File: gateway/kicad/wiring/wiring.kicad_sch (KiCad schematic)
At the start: 1 part

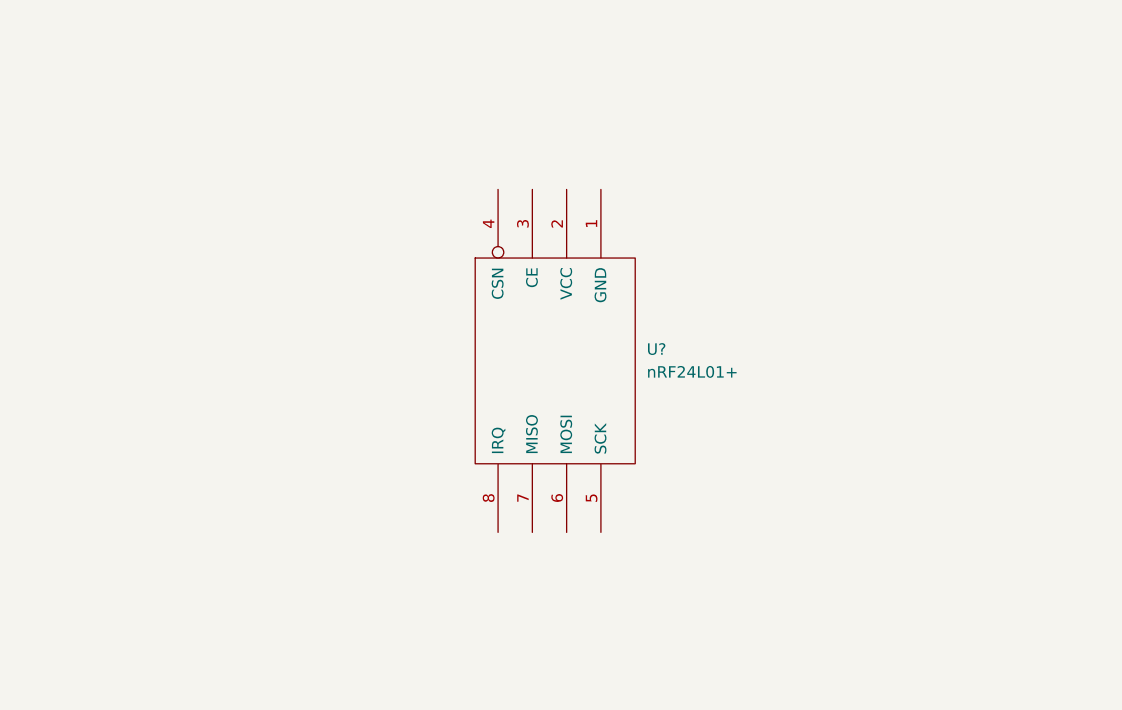
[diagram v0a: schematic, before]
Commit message: feat: wiring for gateway
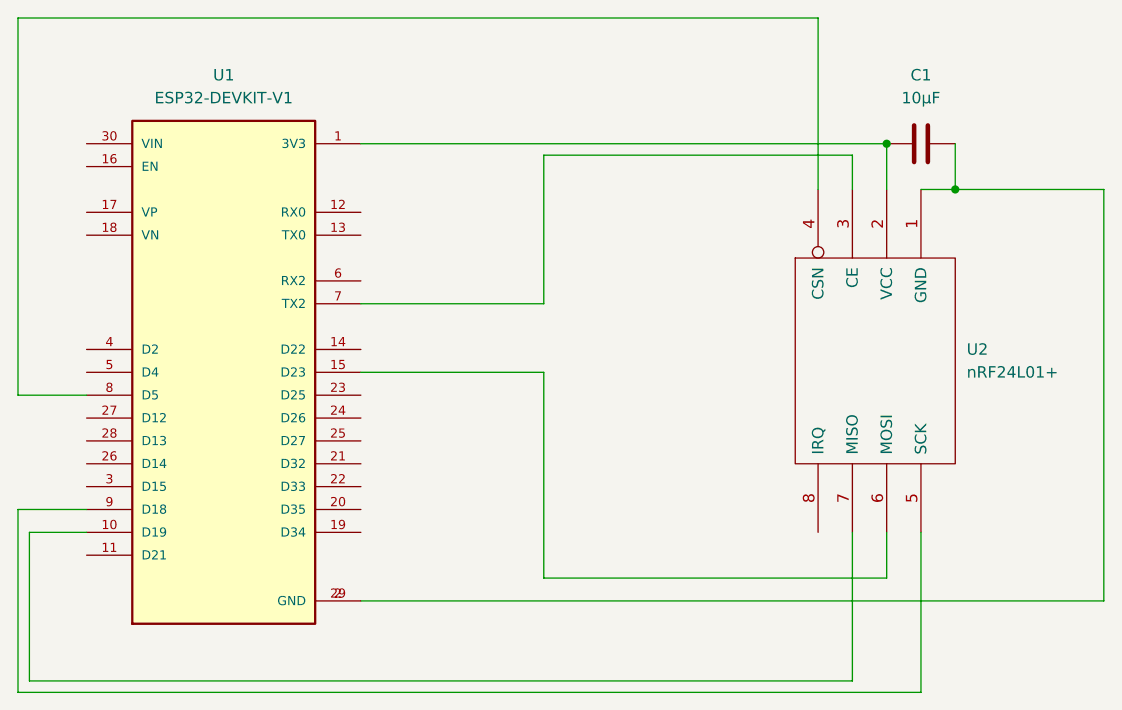
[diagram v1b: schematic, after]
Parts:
- added C1: 10µF, Capacitor_THT:C_Disc_D3.0mm_W1.6mm_P2.50mm, symbol Device:C
- added U1: ESP32-DEVKIT-V1, ESP32-DEVKIT-V1:MODULE_ESP32_DEVKIT_V1, symbol ESP32-DEVKIT-V1:ESP32-DEVKIT-V1
- gave numbers to parts that had none: 1
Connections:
- net at U2.1 (GND): now also C1.2, U1.2 (GND), U1.29 (GND)
- net at U2.2 (VCC): now also C1.1, U1.1 (3V3)
- net at U2.3 (CE): now also U1.7 (TX2)
- net at U2.4 (CSN): now also U1.8 (D5)
- net at U2.5 (SCK): now also U1.9 (D18)
- net at U2.6 (MOSI): now also U1.15 (D23)
- net at U2.7 (MISO): now also U1.10 (D19)
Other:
- moved on the sheet: U2
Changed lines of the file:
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@@
 (kicad_sch (version 20211123) (generator eeschema)
   (paper "A4")
-  (symbol (lib_id "nRF24L01+:nRF24L01+") (at 139.7 91.44 270) (unit 1)
+  (junction (at 176.53 67.31) (diameter 0) (color 0 0 0 0)
+  )
+  (junction (at 184.15 72.39) (diameter 0) (color 0 0 0 0)
+  )
+  (wire (pts (xy 138.43 85.09) (xy 138.43 68.58))
+    (stroke (width 0) (type default) (color 0 0 0 0))
+  )
+  (wire (pts (xy 118.11 67.31) (xy 176.53 67.31))
+    (stroke (width 0) (type default) (color 0 0 0 0))
+  )
+  (wire (pts (xy 138.43 92.71) (xy 138.43 115.57))
+    (stroke (width 0) (type default) (color 0 0 0 0))
+  )
+  (wire (pts (xy 172.72 68.58) (xy 172.72 72.39))
+    (stroke (width 0) (type default) (color 0 0 0 0))
+  )
+  (wire (pts (xy 184.15 67.31) (xy 184.15 72.39))
+    (stroke (width 0) (type default) (color 0 0 0 0))
+  )
+  (wire (pts (xy 138.43 68.58) (xy 172.72 68.58))
+    (stroke (width 0) (type default) (color 0 0 0 0))
+  )
+  (wire (pts (xy 200.66 118.11) (xy 200.66 72.39))
+    (stroke (width 0) (type default) (color 0 0 0 0))
+  )
+  (wire (pts (xy 184.15 72.39) (xy 180.34 72.39))
+    (stroke (width 0) (type default) (color 0 0 0 0))
+  )
+  (wire (pts (xy 200.66 72.39) (xy 184.15 72.39))
+    (stroke (width 0) (type default) (color 0 0 0 0))
+  )
+  (wire (pts (xy 118.11 92.71) (xy 138.43 92.71))
+    (stroke (width 0) (type default) (color 0 0 0 0))
+  )
+  (wire (pts (xy 81.28 127) (xy 172.72 127))
+    (stroke (width 0) (type default) (color 0 0 0 0))
+  )
+  (wire (pts (xy 80.01 128.27) (xy 180.34 128.27))
+    (stroke (width 0) (type default) (color 0 0 0 0))
+  )
+  (wire (pts (xy 138.43 115.57) (xy 176.53 115.57))
+    (stroke (width 0) (type default) (color 0 0 0 0))
+  )
+  (wire (pts (xy 176.53 67.31) (xy 176.53 72.39))
+    (stroke (width 0) (type default) (color 0 0 0 0))
+  )
+  (wire (pts (xy 118.11 118.11) (xy 200.66 118.11))
+    (stroke (width 0) (type default) (color 0 0 0 0))
+  )
+  (wire (pts (xy 87.63 110.49) (xy 81.28 110.49))
+    (stroke (width 0) (type default) (color 0 0 0 0))
+  )
+  (wire (pts (xy 81.28 110.49) (xy 81.28 127))
+    (stroke (width 0) (type default) (color 0 0 0 0))
+  )
+  (wire (pts (xy 118.11 85.09) (xy 138.43 85.09))
+    (stroke (width 0) (type default) (color 0 0 0 0))
+  )
+  (wire (pts (xy 80.01 53.34) (xy 168.91 53.34))
+    (stroke (width 0) (type default) (color 0 0 0 0))
+  )
+  (wire (pts (xy 80.01 107.95) (xy 80.01 128.27))
+    (stroke (width 0) (type default) (color 0 0 0 0))
+  )
+  (wire (pts (xy 180.34 128.27) (xy 180.34 110.49))
+    (stroke (width 0) (type default) (color 0 0 0 0))
+  )
+  (wire (pts (xy 172.72 127) (xy 172.72 110.49))
+    (stroke (width 0) (type default) (color 0 0 0 0))
+  )
+  (wire (pts (xy 176.53 110.49) (xy 176.53 115.57))
+    (stroke (width 0) (type default) (color 0 0 0 0))
+  )
+  (wire (pts (xy 80.01 95.25) (xy 80.01 53.34))
+    (stroke (width 0) (type default) (color 0 0 0 0))
+  )
+  (wire (pts (xy 87.63 95.25) (xy 80.01 95.25))
+    (stroke (width 0) (type default) (color 0 0 0 0))
+  )
+  (wire (pts (xy 168.91 53.34) (xy 168.91 72.39))
+    (stroke (width 0) (type default) (color 0 0 0 0))
+  )
+  (wire (pts (xy 87.63 107.95) (xy 80.01 107.95))
+    (stroke (width 0) (type default) (color 0 0 0 0))
+  )
+  (symbol (lib_id "Device:C") (at 180.34 67.31 90) (unit 1)
     (in_bom yes) (on_board yes) (fields_autoplaced)
-    (property "Reference" "U?" (id 0) (at 149.86 90.1699 90)
+    (property "Reference" "C1" (id 0) (at 180.34 59.69 90))
+    (property "Value" "10µF" (id 1) (at 180.34 62.23 90))
+    (property "Footprint" "Capacitor_THT:C_Disc_D3.0mm_W1.6mm_P2.50mm" (id 2) (at 184.15 66.3448 0)
+      (effects (font (size 1.27 1.27)) hide)
+    )
+    (property "Datasheet" "~" (id 3) (at 180.34 67.31 0)
+      (effects (font (size 1.27 1.27)) hide)
+    )
+    (pin "1")
+    (pin "2")
+  )
+  (symbol (lib_id "nRF24L01+:nRF24L01+") (at 175.26 91.44 270) (unit 1)
+    (in_bom yes) (on_board yes) (fields_autoplaced)
+    (property "Reference" "U2" (id 0) (at 185.42 90.1699 90)
       (effects (font (size 1.27 1.27)) (justify left))
     )
-    (property "Value" "nRF24L01+" (id 1) (at 149.86 92.7099 90)
+    (property "Value" "nRF24L01+" (id 1) (at 185.42 92.7099 90)
       (effects (font (size 1.27 1.27)) (justify left))
     )
-    (property "Footprint" "RF_Module:nRF24L01_Breakout" (id 2) (at 142.24 91.44 0)
+    (property "Footprint" "RF_Module:nRF24L01_Breakout" (id 2) (at 177.8 91.44 0)
       (effects (font (size 1.27 1.27)) hide)
     )
-    (property "Datasheet" "DOCUMENTATION" (id 3) (at 138.43 91.44 0)
+    (property "Datasheet" "DOCUMENTATION" (id 3) (at 173.99 91.44 0)
       (effects (font (size 1.27 1.27)) hide)
     )
@@
     (pin "8")
   )
+  (symbol (lib_id "ESP32-DEVKIT-V1:ESP32-DEVKIT-V1") (at 102.87 92.71 0) (unit 1)
+    (in_bom yes) (on_board yes) (fields_autoplaced)
+    (property "Reference" "U1" (id 0) (at 102.87 59.69 0))
+    (property "Value" "ESP32-DEVKIT-V1" (id 1) (at 102.87 62.23 0))
+    (property "Footprint" "ESP32-DEVKIT-V1:MODULE_ESP32_DEVKIT_V1" (id 2) (at 102.87 92.71 0)
+      (effects (font (size 1.27 1.27)) (justify left bottom) hide)
+    )
+    (property "Datasheet" "" (id 3) (at 102.87 92.71 0)
+      (effects (font (size 1.27 1.27)) (justify left bottom) hide)
+    )
+    (property "MAXIMUM_PACKAGE_HEIGHT" "6.8 mm" (id 4) (at 102.87 92.71 0)
+      (effects (font (size 1.27 1.27)) (justify left bottom) hide)
+    )
+    (property "PARTREV" "N/A" (id 5) (at 102.87 92.71 0)
+      (effects (font (size 1.27 1.27)) (justify left bottom) hide)
+    )
+    (property "MANUFACTURER" "DOIT" (id 6) (at 102.87 92.71 0)
+      (effects (font (size 1.27 1.27)) (justify left bottom) hide)
+    )
+    (property "STANDARD" "Manufacturer Recommendations" (id 7) (at 102.87 92.71 0)
+      (effects (font (size 1.27 1.27)) (justify left bottom) hide)
+    )
+    (pin "1")
+    (pin "10")
+    (pin "11")
+    (pin "12")
+    (pin "13")
+    (pin "14")
+    (pin "15")
+    (pin "16")
+    (pin "17")
+    (pin "18")
+    (pin "19")
+    (pin "2")
+    (pin "20")
+    (pin "21")
+    (pin "22")
+    (pin "23")
+    (pin "24")
+    (pin "25")
+    (pin "26")
+    (pin "27")
+    (pin "28")
+    (pin "29")
+    (pin "3")
+    (pin "30")
+    (pin "4")
+    (pin "5")
+    (pin "6")
+    (pin "7")
+    (pin "8")
+    (pin "9")
+  )
   (sheet_instances
     (path "/" (page "1"))
   )
   (symbol_instances
+    (path "/719c44aa-4337-4ee7-8a2d-9f3ea02b1928"
+      (reference "C1") (unit 1) (value "10µF") (footprint "Capacitor_THT:C_Disc_D3.0mm_W1.6mm_P2.50mm")
+    )
+    (path "/e535c008-4307-47fc-a3e4-776f47f273b1"
+      (reference "U1") (unit 1) (value "ESP32-DEVKIT-V1") (footprint "ESP32-DEVKIT-V1:MODULE_ESP32_DEVKIT_V1")
+    )
     (path "/d4286bc5-3f3a-4659-80b9-42b41fa62ce8"
-      (reference "U?") (unit 1) (value "nRF24L01+") (footprint "RF_Module:nRF24L01_Breakout")
+      (reference "U2") (unit 1) (value "nRF24L01+") (footprint "RF_Module:nRF24L01_Breakout")
     )
   )
